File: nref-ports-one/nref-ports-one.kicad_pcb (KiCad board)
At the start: 4 copper layers, 88 x 35.8 mm, 155 parts, among them J1 CONN_HEAD, J10 CONN_SPK, J11 POWSW, J12 SBU, J2 DM3AT-SF-PEJM5, J3 09452812561, J4 USB_C_Receptacle, J5 Conn_01x10_Pin, J6 Conn_01x14_Pin, J7 Conn_01x12_Pin, J8 PWR, J9 Conn_01x10_Pin, SW1 SW_Push, U1 TPS7A0533PDBZ, U10 LMR51430, U11 TPS66021YBGR, U12 TLV75518PDBV, U13 TMUXHS4212, U14 EQCO5X31C0-I_6NX, U15 LP5907MFX-1.2, U2 TLV320AIC3100, U3 TXS0108EPW, U4 SN74AVC1T45, U5 TPD4E02B04DQA, U6 TPD4E02B04DQA, U7 TPD4E02B04DQA, U8 FUSB302BMPX, U9 PCA9557RGVR

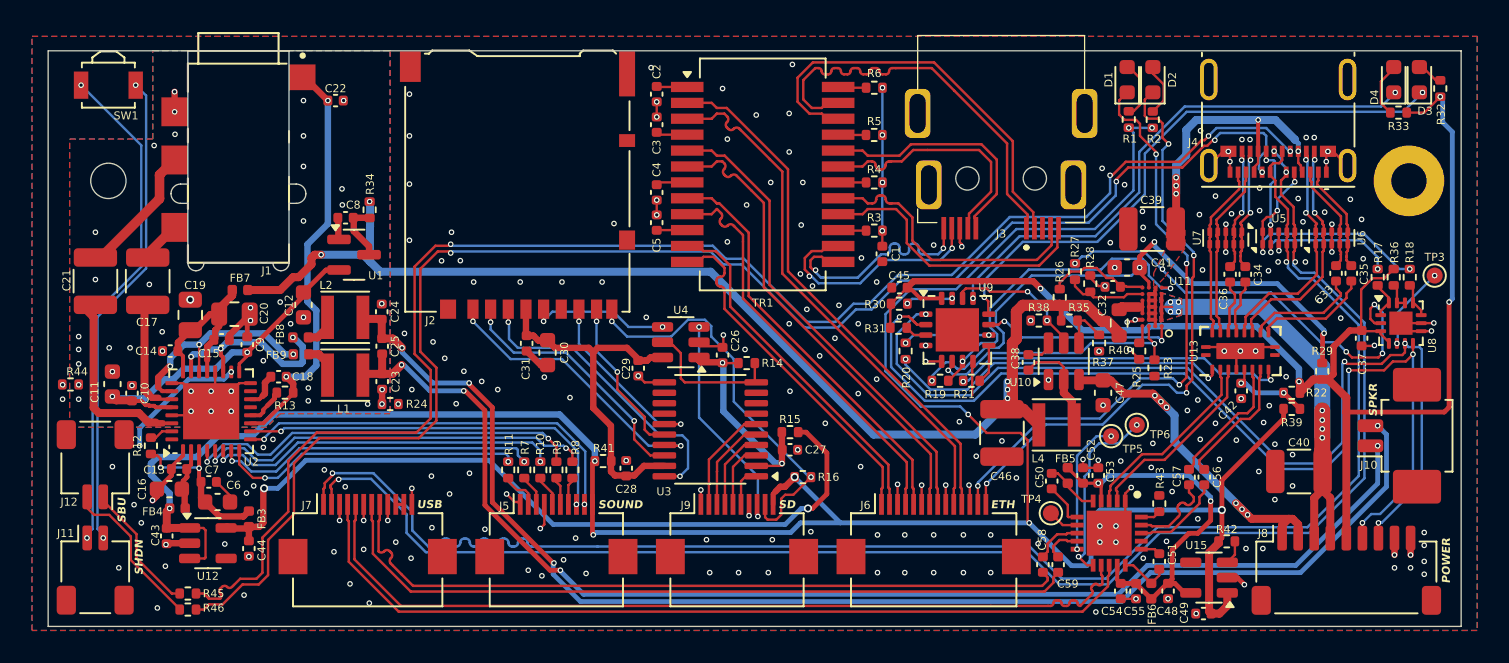
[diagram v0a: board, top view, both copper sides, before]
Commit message: ports-one: fix u9 pinout; remove r23
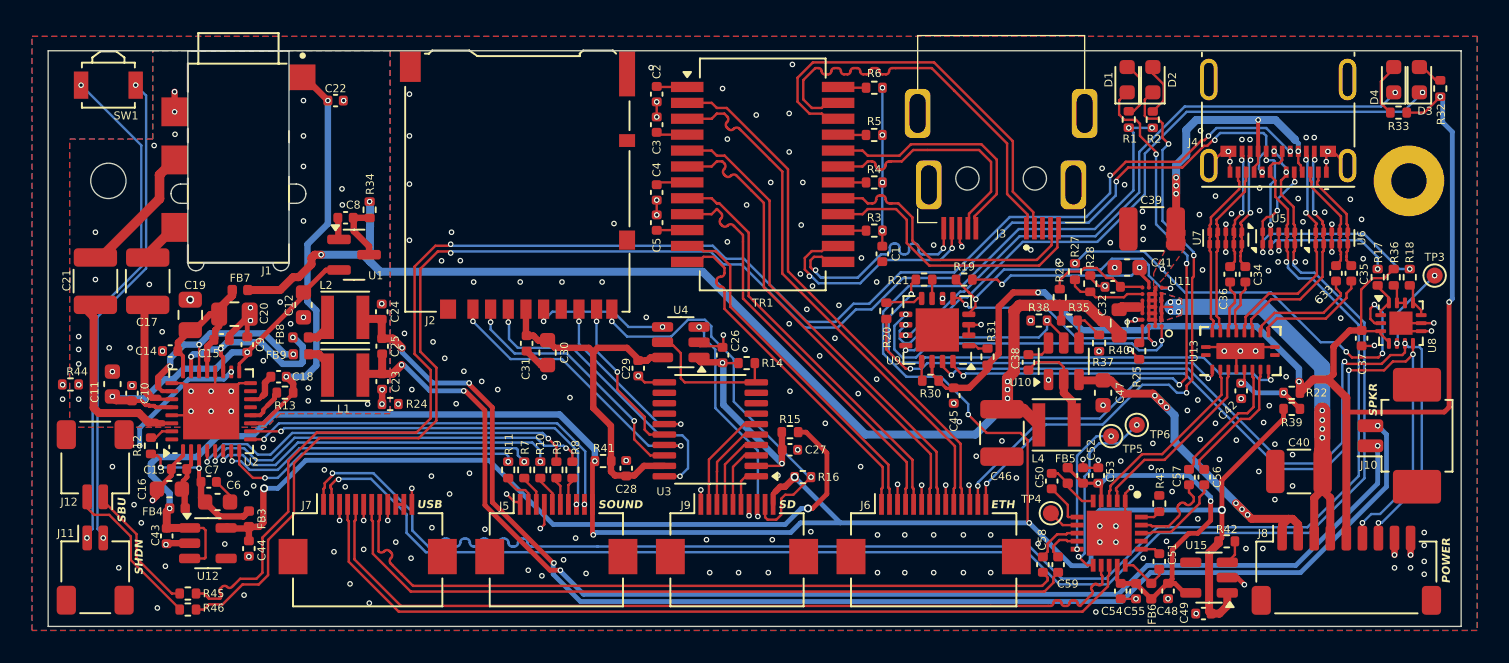
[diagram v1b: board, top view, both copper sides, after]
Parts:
- removed R23: 10k, Resistor_SMD:R_0402_1005Metric
- removed R29: 0, Resistor_SMD:R_0402_1005Metric
- moved C45 7.52 mm to (156.4, 123.4), turned to -90 degrees
- moved R21 6.96 mm to (154.6, 116.2)
- moved R19 6.48 mm to (157.1, 116.2), turned to 0 degrees
- moved R31 5.83 mm to (158.5, 121.0), turned to 90 degrees
- moved R30 5.18 mm to (154.9, 122.5), turned to 180 degrees
- moved R20 2.77 mm to (152.2, 118.1)
- moved U9 1.25 mm to (155.4, 119.3), turned to 180 degrees
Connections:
- net LDO_3V3 renamed LDO_5V
- U9 pad 1: RP_SCL0 -> Net-(U9-A0)
- U9 pad 10: ~{USB_MUX_OE} -> Net-(D3-K)
- U9 pad 11: ~{USB_FAULT} -> Net-(D4-K)
- U9 pad 12: Net-(D3-K) -> 5V_AUX_EN
- U9 pad 13: Net-(D4-K) -> Net-(U9-~{RESET})
- U9 pad 14: 5V_AUX_EN -> STANDBY_3V3
- U9 pad 15: Net-(U9-~{RESET}) -> RP_SCL0
- U9 pad 16: STANDBY_3V3 -> RP_SDA0
- U9 pad 2: RP_SDA0 -> GND
- U9 pad 3: Net-(U9-A0) -> GND
- U9 pad 4: GND -> USB_SINK_EN
- U9 pad 5: GND -> USB_SRC_EN
- U9 pad 6: USB_SRC_EN -> GND
- U9 pad 7: USB_SINK_EN -> USB_MUX_DIR
- U9 pad 8: GND -> ~{USB_MUX_OE}
- U9 pad 9: USB_MUX_DIR -> ~{USB_FAULT}
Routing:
- net LDO_5V: track 36.7 -> 12.5 mm, vias 4 -> 2
- net RP_SDA0: track 61.6 -> 51.1 mm
- net Net-(U13-SEL): track 21.0 -> 30.7 mm
- net ~{USB_FAULT}: track 12.2 -> 21.2 mm
- net RP_SCL0: track 60.4 -> 52.6 mm
- net Net-(D3-K): track 35.8 -> 41.6 mm
- net Net-(D4-K): track 33.6 -> 38.2 mm
- net 5V_AUX_EN: track 8.79 -> 12.0 mm
- net ~{USB_MUX_OE}: track 5.40 -> 2.33 mm, vias 2 -> 0
- net USB_SINK_EN: track 20.7 -> 17.7 mm
- net Net-(U13-~{OE}): track 21.6 -> 23.7 mm
- net STANDBY_3V3: track 86.8 -> 84.9 mm
- net Net-(U9-~{RESET}): track 2.99 -> 1.22 mm, vias 2 -> 0
- net GND: track 74.7 -> 73.0 mm, vias 231 -> 234
- net USB_SRC_EN: track 16.7 -> 15.0 mm
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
